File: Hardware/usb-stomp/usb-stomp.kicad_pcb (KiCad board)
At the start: 4 copper layers, 48 x 48 mm, 30 parts, among them J1 Conn_01x12_MountingPin, J2 USB_C_Receptacle_USB2.0_16P, J3 BM28B0.6-24DS/2, J4 AudioJack4, J5 AudioJack4, J6 I2C1, SW1 SW_SPST, U1 TLV76733DRVx, U2 USBLC6-2P6, U3 74AHCT1G125, U4 TLP2310

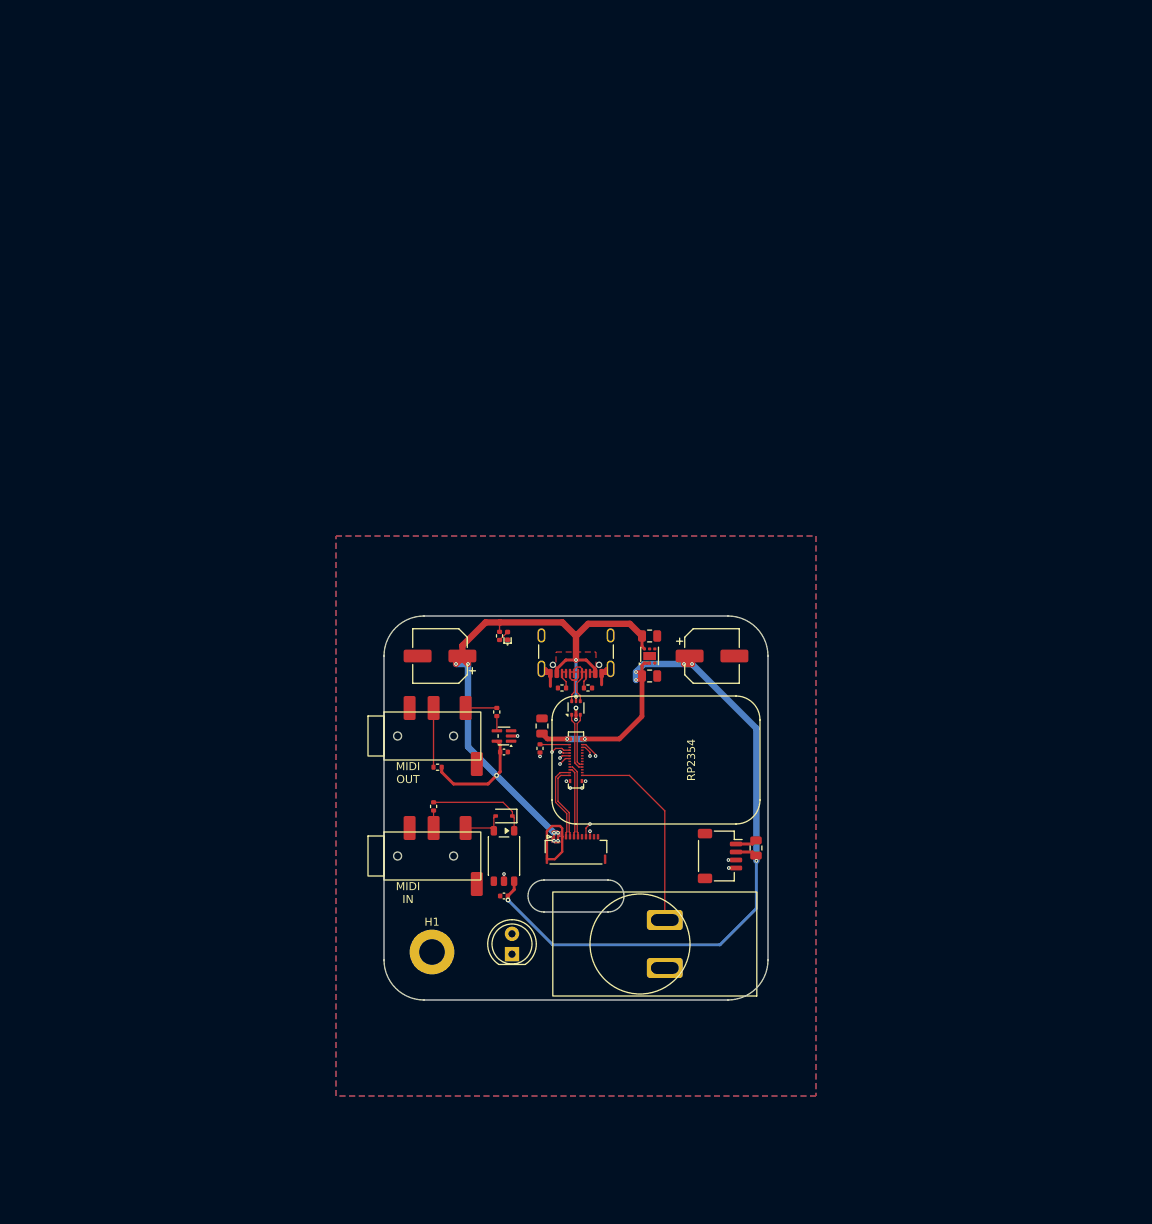
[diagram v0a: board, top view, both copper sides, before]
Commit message: Update the "USB Stomp" board to use design blocks
This is pretty much a re-do of the "USB Stomp" board to include
everything into one single design and one single resulting board.

It makes little sense - it's not that interesting a board - but the
impetus was mostly just to learn and use new features, both on the
design side and on the manufacturing side.

So this does two very big things:

 - it uses the new TAC5242 / RP2354 design blocks as part of the
   schematic and the PCB layout.

 - the board is manufactured as one single flex board instead of having
   separate "audio jacks" and "USB stomp" boards

In other words, it's the same as the combination of the "audio jacks"
board and the previous "USB stomp" board, that used a FFC cable to
connect the two, except now the FFC cable is basically part of the
design, and the traditional rigid parts have been replaced by FR4
stiffeners instead.

In the process, this does various other minor changes:

 - No more separate BOOTSEL switch, which was a nightmare when the thing
   was boxed up. Instead, the stomp switch doubles up as the BOOTSEL
   switch too.

   Connecting the same switch to both a GPIO and BOOTSEL needs a bit of
   care: it would have been technically possible to only connect it to
   the the BOOTSEL pin, and read it that way with no GPIO at all, but
   the BOOTSEL line is also tied to the QSPI chip select pin, so then
   reading just the status requires turning off FLASH access.

   I considered doing exactly that, and it is entirely possible to do
   (micropython even has a "rp2.bootsel_button()" function for this),
   but when you use both cores, it's just very painful to make sure
   neither core is accessing the flash while you read the BOOTSEL
   status.

   So adding a little bit of hardware makes it much easier, and isolates
   the GPIO from the QSPI chip select using a dual diode. The switch
   pulls both low, but the wiggling of the QSPI CS line doesn't affect
   the GPIO.

   While at it, this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
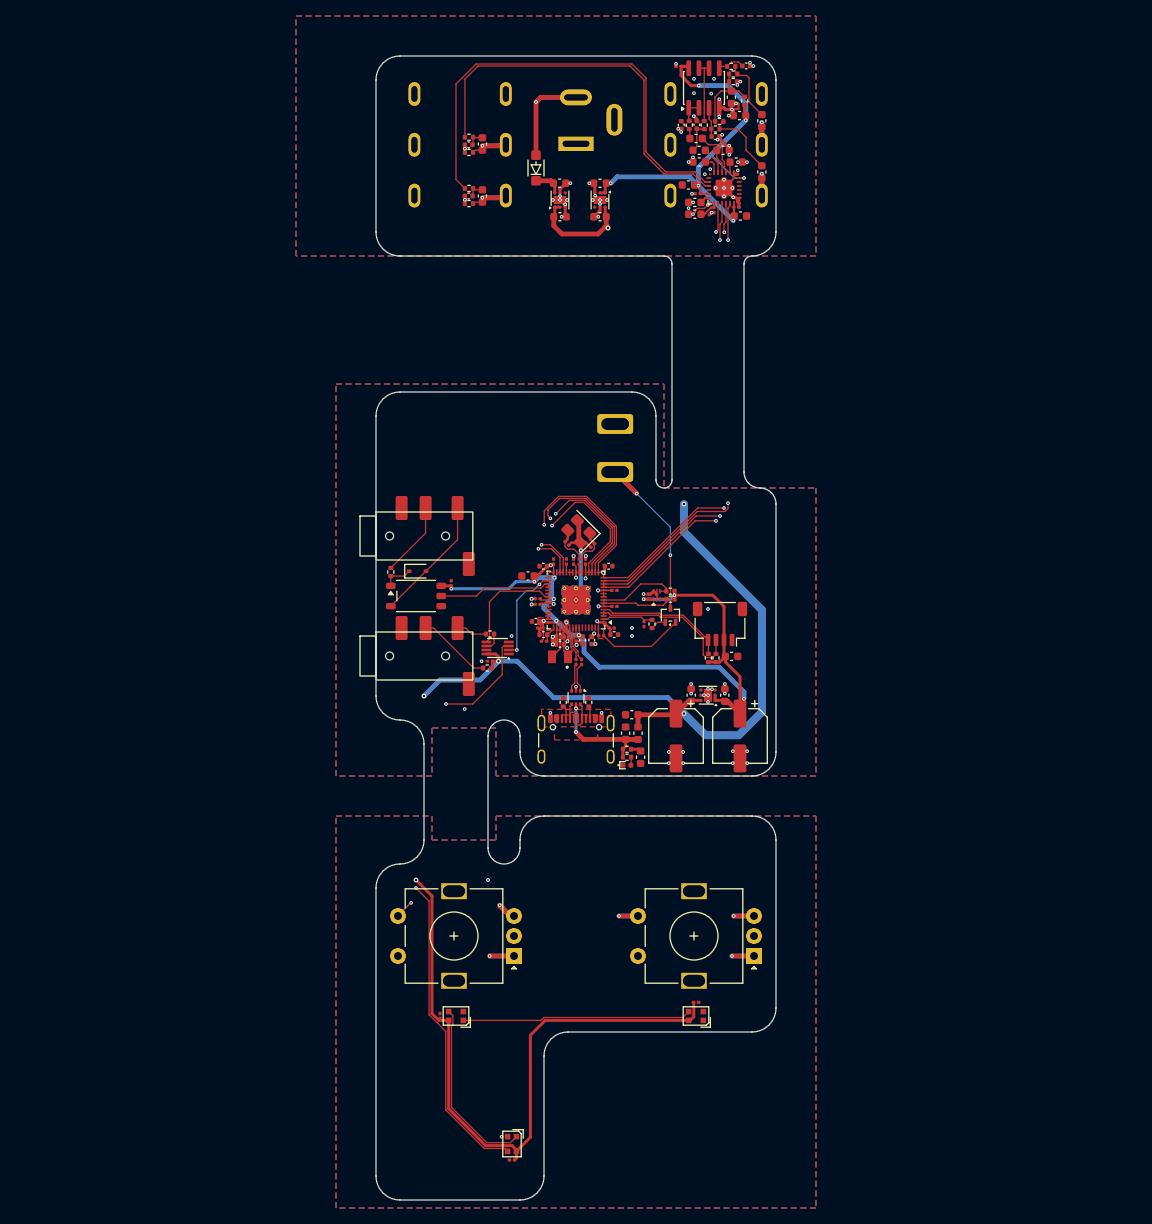
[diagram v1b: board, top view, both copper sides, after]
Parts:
- removed H1: MountingHole_Pad, MountingHole:MountingHole_3.2mm_M3_DIN965_Pad
- removed J3: BM28B0.6-24DS/2, Mylib:BM28B0.6-24DS
- removed J4: AudioJack4, Mylib:PJ-320D
- added C10: 0.1uF, Capacitor_SMD:C_0201_0603Metric, F.Cu at (84.4, 95.9)
- added C101: 2.2nF, Capacitor_SMD:C_0402_1005Metric, F.Cu at (86.6, 47.5)
- added C102: 2.2nF, Capacitor_SMD:C_0402_1005Metric, F.Cu at (86.6, 41.1)
- added C103: 2.2uF, Capacitor_SMD:C_0603_1608Metric, F.Cu at (88.3, 47.5)
- added C104: 2.2uF, Capacitor_SMD:C_0603_1608Metric, F.Cu at (88.3, 41.0)
- added C11: 0.1uF, Capacitor_SMD:C_0201_0603Metric, F.Cu at (89.2, 105.7)
- added C12: 47uF, Capacitor_SMD:CP_Elec_6.3x5.9, F.Cu at (120.5, 115.0)
- added C126: 2.2uF, Capacitor_SMD:C_0603_1608Metric, F.Cu at (103.0, 50.1)
- added C127: 2.2uF, Capacitor_SMD:C_0603_1608Metric, F.Cu at (103.0, 45.9)
- added C128: 0.1uF, Capacitor_SMD:C_0201_0603Metric, F.Cu at (108.5, 101.0)
- added C13: 47uF, Capacitor_SMD:CP_Elec_6.3x5.9, F.Cu at (112.5, 115.0)
- added C14: 2.2uF, Capacitor_SMD:C_0603_1608Metric, F.Cu at (119.5, 105.0)
- added C15: 0.1uF, Capacitor_SMD:C_0201_0603Metric, F.Cu at (109.0, 97.6)
- added C201: 0.1uF, Capacitor_SMD:C_0201_0603Metric, F.Cu at (92.0, 168.0)
- added C202: 0.1uF, Capacitor_SMD:C_0201_0603Metric, F.Cu at (83.0, 150.0)
- added C203: 0.1uF, Capacitor_SMD:C_0201_0603Metric, F.Cu at (115.0, 148.3)
- added C301: 2.2uF, Capacitor_SMD:C_0603_1608Metric, F.Cu at (119.4, 35.1)
- added C302: 2.2uF, Capacitor_SMD:C_0603_1608Metric, F.Cu at (123.2, 44.5)
- added C303: 2.2uF, Capacitor_SMD:C_0603_1608Metric, F.Cu at (123.2, 38.1)
- added C304: 0.1uF, Capacitor_SMD:C_0201_0603Metric, F.Cu at (112.8, 31.3)
- added C305: 150pF, Capacitor_SMD:C_0402_1005Metric, F.Cu at (117.4, 40.1)
- added C306: 150pF, Capacitor_SMD:C_0402_1005Metric, F.Cu at (121.3, 31.2)
- added C307: 2.2nF, Capacitor_SMD:C_0402_1005Metric, F.Cu at (113.2, 38.6)
- added C308: 2.2nF, Capacitor_SMD:C_0402_1005Metric, F.Cu at (115.1, 38.6)
- added C309: 2.2uF, Capacitor_SMD:C_0603_1608Metric, F.Cu at (115.0, 40.3)
- added C310: 2.2uF, Capacitor_SMD:C_0603_1608Metric, F.Cu at (118.4, 41.8)
- added C311: 2.2uF, Capacitor_SMD:C_0603_1608Metric, F.Cu at (115.4, 41.8)
- added C312: 2.2uF, Capacitor_SMD:C_0603_1608Metric, F.Cu at (115.4, 43.2)
- added C313: 10uF, Capacitor_SMD:C_0603_1608Metric, F.Cu at (120.5, 50.0)
- added C314: 10uF, Capacitor_SMD:C_0603_1608Metric, F.Cu at (114.8, 49.8)
- added C315: 2.2uF, Capacitor_SMD:C_0603_1608Metric, F.Cu at (114.8, 48.3)
- added C316: 2.2uF, Capacitor_SMD:C_0603_1608Metric, F.Cu at (120.0, 43.3)
- added C317: 0.1uF, Capacitor_SMD:C_0201_0603Metric, F.Cu at (117.2, 49.2)
- added C318: 10uF, Capacitor_SMD:C_0603_1608Metric, F.Cu at (114.0, 46.1)
- added C319: 10uF, Capacitor_SMD:C_0603_1608Metric, F.Cu at (120.5, 37.5)
- added C320: 0.1uF, Capacitor_SMD:C_0201_0603Metric, F.Cu at (120.0, 48.9)
- added C321: 0.1uF, Capacitor_SMD:C_0201_0603Metric, F.Cu at (115.2, 47.2)
- added C401: 4.7uF, Capacitor_SMD:C_0402_1005Metric, F.Cu at (98.0, 102.6)
- added C402: 4.7uF, Capacitor_SMD:C_0402_1005Metric, F.Cu at (98.0, 103.5)
- added C403: 4.7uF, Capacitor_SMD:C_0402_1005Metric, F.Cu at (102.0, 103.0)
- added C404: 0.1uF, Capacitor_SMD:C_0201_0603Metric, F.Cu at (95.2, 98.5)
- added C405: 4.7uF, Capacitor_SMD:C_0402_1005Metric, F.Cu at (95.9, 102.3)
- added C406: 0.1uF, Capacitor_SMD:C_0201_0603Metric, F.Cu at (104.8, 98.8)
- added C407: 0.1uF, Capacitor_SMD:C_0201_0603Metric, F.Cu at (99.7, 93.2)
- added C408: 0.1uF, Capacitor_SMD:C_0201_0603Metric, F.Cu at (101.2, 93.2)
- added C409: 0.1uF, Capacitor_SMD:C_0201_0603Metric, F.Cu at (100.0, 102.8)
- added C410: 0.1uF, Capacitor_SMD:C_0201_0603Metric, F.Cu at (104.5, 101.5)
- added C411: 0.1uF, Capacitor_SMD:C_0201_0603Metric, F.Cu at (95.2, 97.8)
- added C412: 0.1uF, Capacitor_SMD:C_0201_0603Metric, F.Cu at (104.8, 96.8)
- added C413: 4.7uF, Capacitor_SMD:C_0402_1005Metric, F.Cu at (100.8, 103.0)
- added C414: 0.1uF, Capacitor_SMD:C_0201_0603Metric, F.Cu at (97.2, 93.2)
- added C415: 4.7uF, Capacitor_SMD:C_0402_1005Metric, F.Cu at (104.8, 102.3)
- added C416: 0.1uF, Capacitor_SMD:C_0201_0603Metric, F.Cu at (95.5, 101.5)
- added C417: 4.7uF, Capacitor_SMD:C_0402_1005Metric, F.Cu at (95.9, 93.8)
- added C418: 15pF, Capacitor_SMD:C_0201_0603Metric, F.Cu at (102.1, 91.2)
- added C419: 15pF, Capacitor_SMD:C_0201_0603Metric, F.Cu at (98.9, 90.9)
- added C420: 4.7uF, Capacitor_SMD:C_0402_1005Metric, F.Cu at (104.1, 93.8)
- added C421: 4.7uF, Capacitor_SMD:C_0402_1005Metric, F.Cu at (95.0, 100.7)
- added D101: BAT54CW, Package_TO_SOT_SMD:SOT-323_SC-70, F.Cu at (111.8, 99.9)
- added D102: WS2812B-2020-V6, LED_SMD:LED_WS2812B-2020_PLCC4_2.0x2.0mm, F.Cu at (92.0, 166.0)
- added D103: WS2812B-2020-V6, LED_SMD:LED_WS2812B-2020_PLCC4_2.0x2.0mm, F.Cu at (85.0, 150.0)
- added D201: WS2812B-2020-V6, LED_SMD:LED_WS2812B-2020_PLCC4_2.0x2.0mm, F.Cu at (115.0, 150.0)
- added FB1: BLM18PG, Inductor_SMD:L_0603_1608Metric, F.Cu at (107.8, 114.7)
- added J301: AudioJack3_SwitchTR, Mylib:NRJ6HM-1-PRE, B.Cu at (116.0, 30.0)
- added J7: AudioJack3_SwitchTR, Mylib:NRJ6HM-1-PRE, B.Cu at (84.0, 30.0)
- added J8: I2C1, Connector_JST:JST_SH_SM04B-SRSS-TB_1x04-1MP_P1.00mm_Horizontal, F.Cu at (118.0, 101.0)
- added L401: 3.3uH, Mylib:AOTA-B2016, F.Cu at (98.0, 105.1)
- added R101: 1k, Resistor_SMD:R_0402_1005Metric, F.Cu at (86.6, 46.5)
- added R102: 1k, Resistor_SMD:R_0402_1005Metric, F.Cu at (86.6, 40.1)
- added R103: 1MEG, Resistor_SMD:R_0402_1005Metric, F.Cu at (86.6, 48.5)
- added R104: 1MEG, Resistor_SMD:R_0402_1005Metric, F.Cu at (86.6, 42.0)
- added R105: 5k1, Resistor_SMD:R_0402_1005Metric, F.Cu at (111.8, 97.9)
- added R106: 5k1, Resistor_SMD:R_0402_1005Metric, F.Cu at (111.8, 96.9)
- added R113: 1k, Resistor_SMD:R_0402_1005Metric, F.Cu at (109.5, 101.0)
- added R301: 1MEG, Resistor_SMD:R_0402_1005Metric, F.Cu at (121.1, 35.6)
- added R302: 1MEG, Resistor_SMD:R_0402_1005Metric, F.Cu at (119.7, 33.2)
- added R303: 1MEG, Resistor_SMD:R_0402_1005Metric, F.Cu at (117.9, 38.2)
- added R304: 1MEG, Resistor_SMD:R_0402_1005Metric, F.Cu at (119.7, 32.2)
- added R305: 100R, Resistor_SMD:R_0402_1005Metric, F.Cu at (117.4, 39.1)
- added R306: 100R, Resistor_SMD:R_0402_1005Metric, F.Cu at (119.4, 31.3)
- added R307: 100R, Resistor_SMD:R_0402_1005Metric, F.Cu at (114.2, 38.6)
- added R308: 100R, Resistor_SMD:R_0402_1005Metric, F.Cu at (116.0, 38.6)
- added R401: 33R, Resistor_SMD:R_0201_0603Metric, F.Cu at (96.0, 103.2)
- added R402: 1k, Resistor_SMD:R_0201_0603Metric, F.Cu at (103.2, 102.5)
- added R403: 1k, Resistor_SMD:R_0201_0603Metric, F.Cu at (98.8, 93.2)
- added R404: 33R, Resistor_SMD:R_0201_0603Metric, F.Cu at (100.7, 105.8)
- added R405: 33R, Resistor_SMD:R_0201_0603Metric, F.Cu at (100.0, 105.8)
- added R406: 1k, Resistor_SMD:R_0201_0603Metric, F.Cu at (100.4, 93.2)
- added R8: 5k1, Resistor_SMD:R_0402_1005Metric, F.Cu at (117.5, 105.2)
- added R9: 5k1, Resistor_SMD:R_0402_1005Metric, F.Cu at (116.5, 105.2)
- added SW101: RotaryEncoder_Switch_MP, Rotary_Encoder:RotaryEncoder_Alps_EC11E-Switch_Vertical_H20mm, F.Cu at (92.2, 142.5)
- added SW102: RotaryEncoder_Switch_MP, Rotary_Encoder:RotaryEncoder_Alps_EC11E-Switch_Vertical_H20mm, F.Cu at (122.2, 142.5)
- added U103: TLV76733DRVx, Package_SON:WSON-6-1EP_2x2mm_P0.65mm_EP1x1.6mm, F.Cu at (103.0, 48.0)
- added U201: 74AHCT2G125, Package_SO:VSSOP-8_2.3x2mm_P0.5mm, F.Cu at (90.2, 104.0)
- added U301: OPA2365AIDR, Package_SO:SOIC-8_3.9x4.9mm_P1.27mm, F.Cu at (116.0, 34.0)
- added U302: TAC5242, Mylib:TAC5242, F.Cu at (118.5, 46.5)
- added U401: RP2354A, Package_DFN_QFN:QFN-60-1EP_7x7mm_P0.4mm_EP3.4x3.4mm_ThermalVias, F.Cu at (100.0, 98.0)
- added U6: M24C64-FMH6TG, Mylib:UFDFPN5, F.Cu at (110.1, 97.4)
- added Y401: ABM8-272-T3, Crystal:Crystal_SMD_3225-4Pin_3.2x2.5mm, F.Cu at (100.3, 89.5)
- C1, C2, C3: footprint Capacitor_SMD:C_0805_2012Metric -> Capacitor_SMD:C_0603_1608Metric
- C4, C5: value 47uF -> 2.2uF; footprint Capacitor_SMD:CP_Elec_6.3x5.9 -> Capacitor_SMD:C_0603_1608Metric
- C6, C7: value 0.1uF -> 2.2uF; footprint Capacitor_SMD:C_0402_1005Metric -> Capacitor_SMD:C_0603_1608Metric
- C8: value 2.2uF -> 10uF; footprint Capacitor_SMD:C_0805_2012Metric -> Capacitor_SMD:C_0603_1608Metric
- D1: value LED -> SM4007PL; footprint LED_SMD:LED_0402_1005Metric -> Mylib:SOD-123FL
- D2: value 1N4148WS -> LED; footprint Diode_SMD:D_SOD-323 -> LED_SMD:LED_0402_1005Metric
- D3: value LED -> 1N4148WS; footprint LED_THT:LED_D5.0mm_FlatTop -> Diode_SMD:D_SOD-323
- J1: value Conn_01x12_MountingPin -> USB_C_Receptacle_USB2.0_16P; footprint Mylib:AFH-5-S12FIA-1H -> Connector_USB:USB_C_Receptacle_GCT_USB4105-xx-A_16P_TopMnt_Horizontal
- J2: value USB_C_Receptacle_USB2.0_16P -> Barrel_Jack_Switch; footprint Connector_USB:USB_C_Receptacle_GCT_USB4105-xx-A_16P_TopMnt_Horizontal -> Mylib:Wurth WR-DC 2.1mm Power Jack; moved to B.Cu
- J6: value I2C1 -> AudioJack4; footprint Connector_JST:JST_SH_SM04B-SRSS-TB_1x04-1MP_P1.00mm_Horizontal -> Mylib:PJ-320D
- R3: value 1k -> 1R
- R4: value 220 -> 1k
- R7: value 1k -> 220
- SW1: moved to B.Cu
- U2: value USBLC6-2P6 -> TLV76750DRVx; footprint Package_TO_SOT_SMD:SOT-666 -> Package_SON:WSON-6-1EP_2x2mm_P0.65mm_EP1x1.6mm
- U3: value 74AHCT1G125 -> USBLC6-2P6; footprint Package_TO_SOT_SMD:SOT-353_SC-70-5 -> Package_TO_SOT_SMD:SOT-666
- moved C7 85.2 mm to (98.0, 50.1)
- moved C6 71.4 mm to (98.0, 45.9), turned to 0 degrees
- moved U2 63.5 mm to (98.0, 48.0)
- moved J2 62.5 mm to (100.0, 41.0), turned to 0 degrees
- moved SW1 62.0 mm to (108.0, 79.0), turned to 0 degrees
- moved D1 58.6 mm to (95.0, 44.0)
- moved J6 49.7 mm to (75.0, 105.0), turned to 0 degrees
- moved D3 49.3 mm to (80.2, 94.4), turned to 0 degrees
- moved U4 34.3 mm to (80.0, 97.5), turned to 0 degrees
- moved R5 25.1 mm to (76.8, 94.5), turned to -90 degrees
- moved C5 25.1 mm to (107.0, 112.3)
- moved J5 25.0 mm to (75.0, 90.0)
- moved R4 24.9 mm to (106.4, 117.7), turned to 0 degrees
- moved R3 21.3 mm to (106.4, 116.7), turned to 0 degrees
- moved C1 18.8 mm to (94.0, 95.0), turned to 180 degrees
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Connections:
- C2 pad 1: VBUS -> +5V
- C4 pad 1: +3V3 -> VBUS
- C5 pad 1: VBUS -> +5V
- C6 pad 1: GND -> +8V
- C6 pad 2: VBUS -> GND
- C7 pad 1: GND -> +5V
- C7 pad 2: +3V3 -> GND
- C8 pad 1: +3V3 -> Net-(C8-Pad1)
- D1 pad 1: GND -> +8V
- D1 pad 2: Net-(D1-A) -> +9V
- D2 pad 1: Net-(D2-K) -> GND
- D3 pad 1: GND -> Net-(D3-K)
- J5 pad R1: Net-(J5-PadR1) -> /MIDI/MIDI_IN
- J5 pad S: GND -> unconnected-(J5-PadS)
- J5 pad T: /MIDI_OUT -> Net-(D3-A)
- R1 pad 1: Net-(J2-CC1) -> Net-(J1-CC1)
- R2 pad 1: Net-(J2-CC2) -> Net-(J1-CC2)
- R3 pad 2: Net-(D1-A) -> Net-(C8-Pad1)
- R4 pad 1: /MIDI_IN -> VBUS
- R4 pad 2: Net-(D2-K) -> Net-(D2-A)
- R5 pad 1: VBUS -> /MIDI/MIDI_IN
- R5 pad 2: Net-(J5-PadR1) -> Net-(D3-K)
- R6 pad 1: Net-(R6-Pad1) -> +5V
- R6 pad 2: /MIDI_OUT -> Net-(J6-PadR1)
- R7 pad 1: /GPIO0 -> Net-(R7-Pad1)
- R7 pad 2: Net-(D3-A) -> /MIDI/MIDI_OUT
- SW1 pad 1: GND -> Net-(SW1-A)
- SW1 pad 2: /GPIO13 -> GND
- U1 pad 6: VBUS -> +5V
- U2 pad 1: /USB-D+ -> +5V
- U2 pad 2: GND -> +5V
- U2 pad 3: /USB-D- -> GND
- U2 pad 4: /USBCONN-D- -> unconnected-(U2-EN-Pad4)
- U2 pad 5: VBUS -> GND
- U2 pad 6: /USBCONN-D+ -> +8V
- U3 pad 1: GND -> /USB-D+
- U3 pad 2: /ADC0 -> GND
- U3 pad 3: GND -> /USB-D-
- U3 pad 4: Net-(R6-Pad1) -> /USBCONN-D-
- U4 pad 1: Net-(D2-K) -> Net-(D3-K)
- U4 pad 3: Net-(D2-A) -> Net-(D3-A)
- U4 pad 5: /ADC1 -> /RP2354/GPIO21
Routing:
- net +5V: track 0.00 -> 257.2 mm, vias 0 -> 6
- net GND: track 23.7 -> 177.1 mm, vias 6 -> 94
- net /RP2354/GPIO15: track 0.00 -> 110.5 mm, vias 0 -> 2
- net /RP2354/GPIO16: track 0.00 -> 95.5 mm, vias 0 -> 2
- net /RP2354/GPIO12: track 0.00 -> 92.7 mm, vias 0 -> 2
- net /RP2354/GPIO13: track 0.00 -> 82.3 mm, vias 0 -> 2
- net /RP2354/GPIO14: track 0.00 -> 82.0 mm, vias 0 -> 2
- net Net-(D102-DIN): track 0.00 -> 77.3 mm, vias 0 -> 2
- net /RP2354/GPIO17: track 0.00 -> 77.0 mm, vias 0 -> 2
- net VBUS: track 87.1 -> 13.9 mm, vias 9 -> 2
- net /OUT1P: track 0.00 -> 57.7 mm
- net /RP2354/GPIO10: track 0.00 -> 57.6 mm, vias 0 -> 2
- net /RP2354/GPIO8: track 0.00 -> 57.3 mm, vias 0 -> 2
- net /RP2354/GPIO9: track 0.00 -> 57.3 mm, vias 0 -> 2
- net /RP2354/GPIO11: track 0.00 -> 56.9 mm, vias 0 -> 2
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- added copper zone on F.Cu, net +1V1
- added copper zone on In2.Cu, net +1V1
- added copper zone on F.Cu, net +3V3
- added copper zone on In1.Cu, net +3V3
- removed copper zone on B.Cu, net VBUS
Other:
- board size 48 x 48 mm -> 50 x 143 mm
- board text removed: "RP2354"
